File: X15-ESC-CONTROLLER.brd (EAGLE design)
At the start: 51.6 x 34.2 mm, 29 parts, among them IC1 OP-AMP, J1 3V3 -SWCLK-GND-SWDIO- NRST, Y1 ECS-80-S-4X

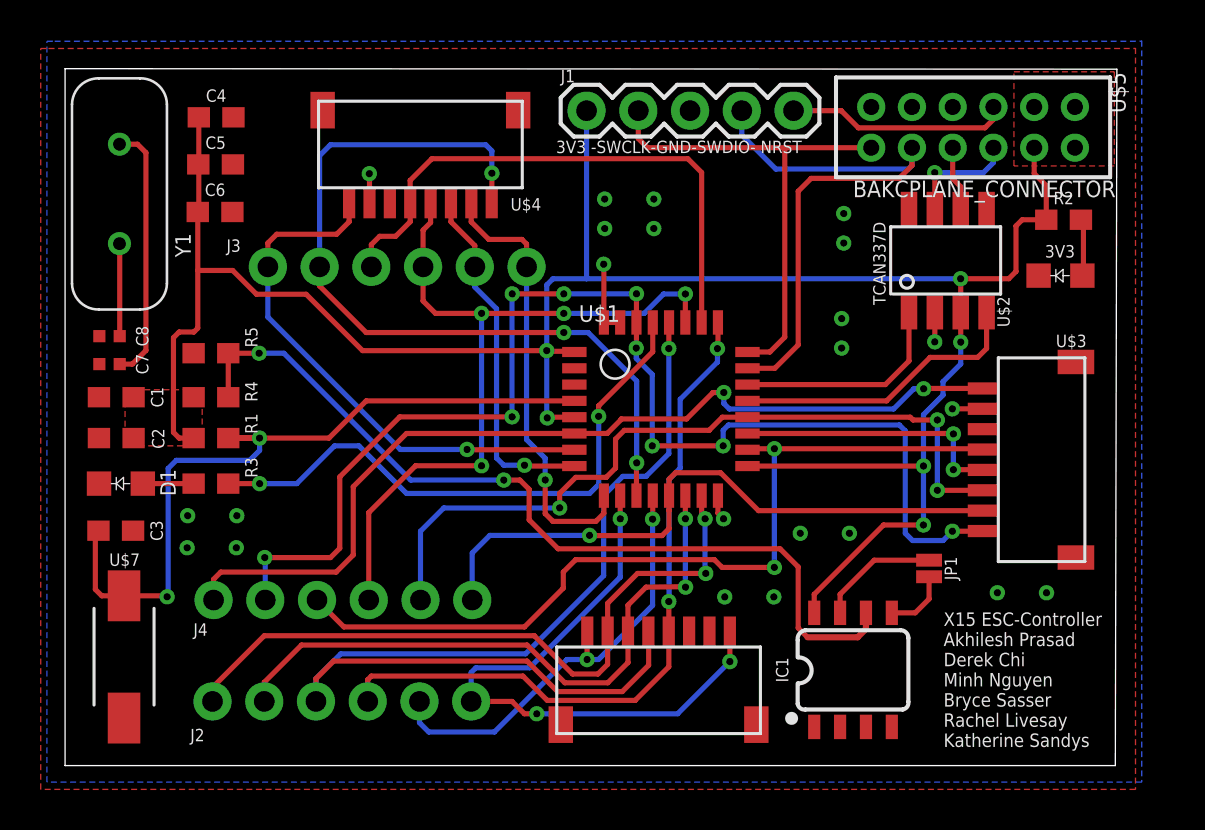
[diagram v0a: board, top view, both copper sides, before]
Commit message: Design X15 ESC Controller Again
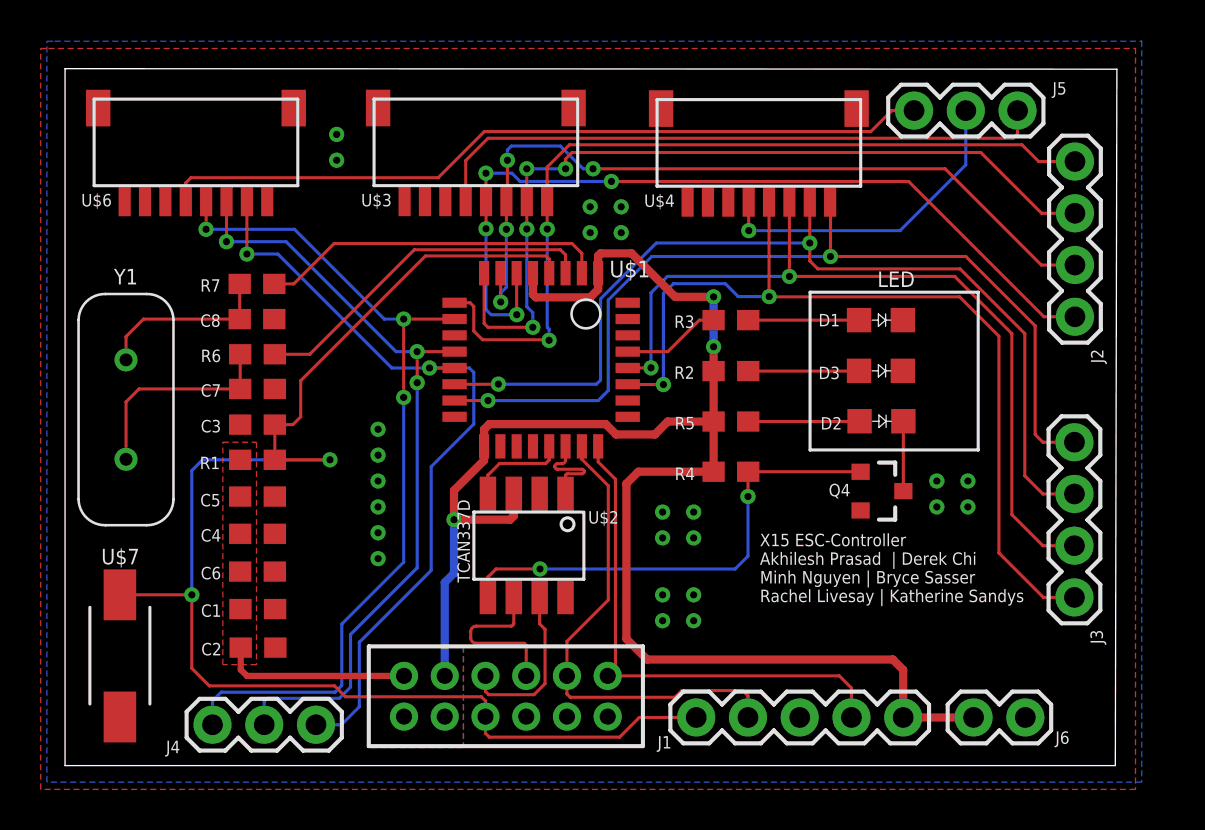
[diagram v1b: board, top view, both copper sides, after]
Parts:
- removed 3V3: COLOR, X15-ESC-Controller-Parts-Library:0805
- removed IC1: OP-AMP, SparkFun-IC-Amplifiers:SO08
- removed JP1: JUMPER-SMT, SparkFun-Jumpers:SMT-JUMPER_2_NO_NO-SILK
- added D2: FAULT, LED-0805:0805
- added D3: PWR, X15-ESC-Controller-Parts-Library:0805
- added J5: (no value), SparkFun-Connectors:1X03
- added J6: (no value), SparkFun-Connectors:1X02
- added Q4: 220mA/50V/3.5Ω, SparkFun-DiscreteSemi:SOT23-3
- added R6, R7: 0, SparkFun-Resistors:0603
- C1, C4, C5, C6: value 0.1uF -> 0.1u
- C2, C3: value 4.7uF -> 4.7u
- C7, C8: value 20pF -> 20p; device SparkFun-Capacitors:0402-TIGHT -> SparkFun-Capacitors:0603
- D1: value COLOR -> PROG
- J1: value 3V3 -SWCLK-GND-SWDIO- NRST -> (none); device X15-ESC-Controller-Parts-Library:1X05 -> SparkFun-Connectors:1X05
- J2, J3: device SparkFun-Connectors:1X06_NO_SILK -> SparkFun-Connectors:1X04
- J4: device SparkFun-Connectors:1X06_NO_SILK -> SparkFun-Connectors:1X03
- R3: value 470 -> 150
- R5: value 3.3k -> 100
- moved J3 42.8 mm to (49.6, 8.26), turned to 90 degrees
- moved U$6 39.8 mm to (1.43, 28.5), turned to 0 degrees
- moved D1 38.2 mm to (40.1, 21.9), turned to 180 degrees
- moved U$5 36.1 mm to (21.6, 3.40), turned to 270 degrees
- moved J2 35.1 mm to (49.6, 22.0), turned to 90 degrees
- moved U$3 31.8 mm to (15.2, 28.5), turned to 0 degrees
- moved J1 30.3 mm to (31.0, 2.36)
- moved R3 26.8 mm to (32.7, 21.9), turned to 0 degrees
- moved R4 25.8 mm to (32.7, 14.4)
- moved R5 25.7 mm to (32.7, 16.9), turned to 180 degrees
- moved C4 20.5 mm to (9.45, 11.4)
- moved U$2 19.1 mm to (24.6, 13.3), turned to 270 degrees
- moved R2 17.9 mm to (32.7, 19.4)
- moved C6 17.8 mm to (9.45, 9.53)
- moved U$4 16.6 mm to (29.1, 28.4)
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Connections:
- net CAN_H renamed CAN_P
- net CAN_L renamed CAN_N
- net N$4 renamed PROG_LED
- removed net ADC_IN0: J4.1, U$1.PA0, U$3.1
- removed net ADC_IN1: J3.1, U$1.PA1, U$4.1
- removed net ADC_IN4: J2.1, U$1.PA4, U$6.1
- removed net ESC_ID: U$5.12
- removed net N$12: U$2.FAULT
- removed net N$6: C7.1, Y1.2
- removed net N$9: U$2.S
- removed net TIM1_CH1: J4.3, U$1.PA8, U$3.4
- removed net TIM1_CH2: U$1.PA9, U$3.5
- removed net TIM1_CH3: J4.5, U$1.PA10, U$3.6
- removed net TLM: IC1.7, JP1.2
- removed net TLM_ESC: IC1.5, JP1.1
- new net FAULT: Q4.1, R4.1, U$2.FAULT
- new net N$4: C7.1, R6.1, Y1.2
- new net OSC_IN: R7.2, U$1.PF0-OSC_IN
- new net OSC_OUT: R6.2, U$1.PF1-OSC_OUT
- new net TIM14_CH1: J4.1, U$1.PA4, U$6.5
- new net TIM3_CH1: J3.1, U$1.PB4, U$4.5
- net +3V3: now also J1.5, J6.2, R5.2; no longer IC1.8, J1.1
- net GND: now also D3.C, J6.1, Q4.2, U$3.MECH1, U$3.MECH2, U$4.MECH1, U$4.MECH2, U$6.MECH1, U$6.MECH2; no longer 3V3.C, IC1.4, R5.1
- net N$1: now also D3.A; no longer 3V3.A
- net N$2: now also D2.C, Q4.3; no longer C3.1, R1.1, U$1.NRST, U$7.2
- net N$3: now also D2.A, R5.1; no longer IC1.6, R4.1, R5.2
- net N$7: now also R7.1
- net NRST: now also C3.1, J1.1, R1.1, U$1.NRST, U$7.2; no longer J1.5
- net SWCLK: now also J1.4; no longer J1.2
- net SWDIO: now also J1.2; no longer J1.4
- net TIM16_CH1: now also J4.2, U$1.PA6, U$6.6; no longer J2.3, U$1.PA15, U$6.4
- net TIM17_CH1: now also J4.3, U$6.7; no longer J4.6, U$3.7
- net TIM2_CH1: now also J2.1, U$1.PA0, U$3.5; no longer J3.3, U$1.PB3, U$4.4
- net TIM2_CH2: now also J2.2, U$1.PA1, U$3.6; no longer J3.4, J4.4, U$1.PB4, U$4.5
- net TIM2_CH3: now also J2.3, U$3.7; no longer J3.5, U$4.6
- net TIM2_CH4: now also J2.4, U$3.8; no longer J3.6, U$4.7
- net TIM3_CH2: now also J3.2, U$4.6; no longer J2.4, U$6.5
- net TIM3_CH3: now also J3.3, U$4.7; no longer J2.5, U$6.6
- net TIM3_CH4: now also J3.4, U$4.8; no longer J2.6, U$6.7
- net TLM_1: now also J5.1, U$3.4; no longer J4.2, U$1.PB7, U$3.8
- net TLM_2: now also J5.2, U$4.4; no longer J3.2, U$1.PA5, U$4.8
- net TLM_3: now also J5.3, U$6.4; no longer J2.2, U$1.PA6, U$6.8
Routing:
- net NRST: track 10.9 -> 70.9 mm, vias 0 -> 2
- net ADC_IN0: track 45.6 -> 0.00 mm, vias 2 -> 0
- net TIM3_CH1: track 0.00 -> 43.9 mm, vias 0 -> 2
- net TIM14_CH1: track 0.00 -> 42.5 mm, vias 0 -> 3
- net TIM1_CH1: track 42.4 -> 0.00 mm, vias 2 -> 0
- net TIM1_CH3: track 38.1 -> 0.00 mm, vias 3 -> 0
- net N$3: track 42.8 -> 5.47 mm, vias 2 -> 0
- net N$2: track 37.7 -> 3.43 mm, vias 2 -> 0
- net TLM_1: track 61.7 -> 30.8 mm, vias 9 -> 0
- net ADC_IN4: track 30.2 -> 0.00 mm, vias 3 -> 0
- net ADC_IN1: track 26.7 -> 0.00 mm, vias 1 -> 0
- net TLM_2: track 40.9 -> 16.1 mm, vias 3 -> 1
- net PROG_LED: track 29.2 -> 4.86 mm, vias 2 -> 0
- net TIM2_CH3: track 17.4 -> 41.6 mm, vias 1 -> 4
- net FAULT: track 0.00 -> 23.8 mm, vias 0 -> 2
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- added copper zone on layer 16, net +3V3
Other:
- board text added: "LED"
- board text added: "X15 ESC-Controller Akhilesh Prasad | Derek Chi Minh Nguyen | Bryce Sasser Rachel Livesay | Katherine Sandys"
- board text removed: "X15 ESC-Controller Akhilesh Prasad Derek Chi Minh Nguyen Bryce Sasser Rachel Livesay Katherine Sandys"

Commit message: Fix New Version of X15-ESC Controller
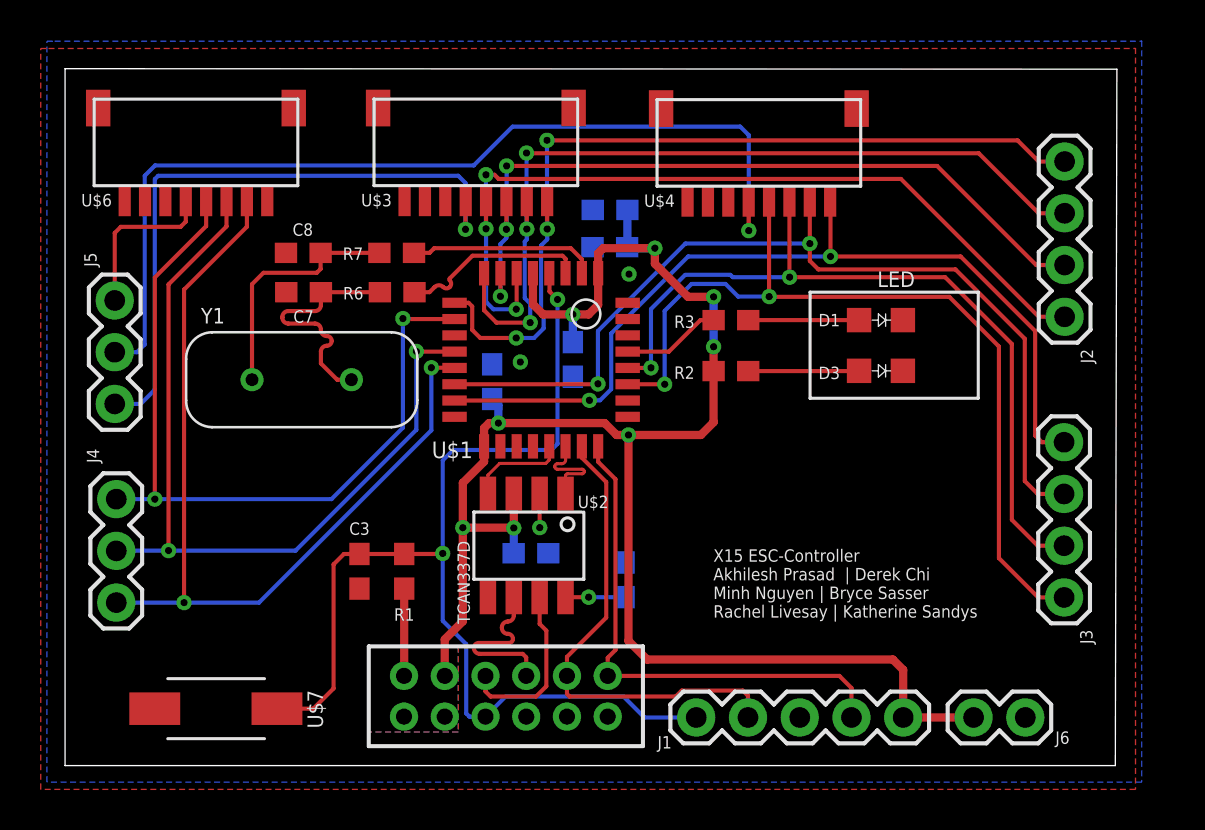
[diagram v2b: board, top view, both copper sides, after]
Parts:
- removed D2: FAULT, LED-0805:0805
- removed Q4: 220mA/50V/3.5Ω, SparkFun-DiscreteSemi:SOT23-3
- removed R5: 100, SparkFun-Resistors:0603
- R4: value 1k -> 0
- moved J5 46.6 mm to (2.44, 17.8), turned to 90 degrees
- moved C2 26.2 mm to (26.7, 25.5), flipped to the bottom, turned to 180 degrees
- moved C1 26.1 mm to (26.8, 27.3), flipped to the bottom
- moved C5 16.9 mm to (24.9, 19.9), flipped to the bottom, turned to 270 degrees
- moved C4 13.7 mm to (21.0, 18.8), flipped to the bottom, turned to 90 degrees
- moved C6 13.5 mm to (22.9, 10.4), flipped to the bottom
- moved J4 12.0 mm to (2.51, 13.1), turned to 270 degrees
- moved R1 9.05 mm to (16.6, 9.54), turned to 270 degrees
- moved C3 8.77 mm to (14.5, 9.54), turned to 270 degrees
- moved Y1 8.75 mm to (11.6, 18.9), turned to 0 degrees
- moved R6 7.50 mm to (16.3, 23.2)
- moved R4 7.44 mm to (27.5, 9.12), flipped to the bottom, turned to 270 degrees
- moved R7 7.03 mm to (16.3, 25.2)
- moved U$7 5.38 mm to (7.40, 2.79), turned to 0 degrees
- moved C7 5.26 mm to (11.7, 23.2), turned to 180 degrees
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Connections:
- removed net FAULT: Q4.1, R4.1, U$2.FAULT
- removed net N$3: D2.A, R5.1
- net +3V3: now also C2.2, C5.1, C6.2; no longer C2.1, C5.2, C6.1, R4.2, R5.2
- net GND: now also C2.1, C5.2, C6.1, R4.1; no longer C2.2, C5.1, C6.2, Q4.2
- net N$2: now also R4.2, U$2.S; no longer D2.C, Q4.3
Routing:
- net TLM_2: track 16.1 -> 46.9 mm
- net TLM_3: track 38.1 -> 8.05 mm
- net FAULT: track 23.8 -> 0.00 mm, vias 2 -> 0
- net NRST: track 70.9 -> 54.5 mm
- net OSC_OUT: track 17.4 -> 9.18 mm
- net OSC_IN: track 17.1 -> 9.25 mm
- net TIM17_CH1: track 38.6 -> 44.2 mm
- net N$3: track 5.47 -> 0.00 mm
- net TIM14_CH1: track 42.5 -> 39.1 mm, vias 3 -> 2
- net N$7: track 8.81 -> 12.0 mm
- net TIM16_CH1: track 38.9 -> 41.3 mm, vias 3 -> 2
- net GND: track 0.00 -> 1.67 mm, vias 24 -> 3
- net TIM3_CH4: track 45.6 -> 43.9 mm
- net N$4: track 10.4 -> 11.8 mm
- net TIM3_CH3: track 47.4 -> 46.1 mm
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
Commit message: Complete New Version of X15 ESC Controller Board
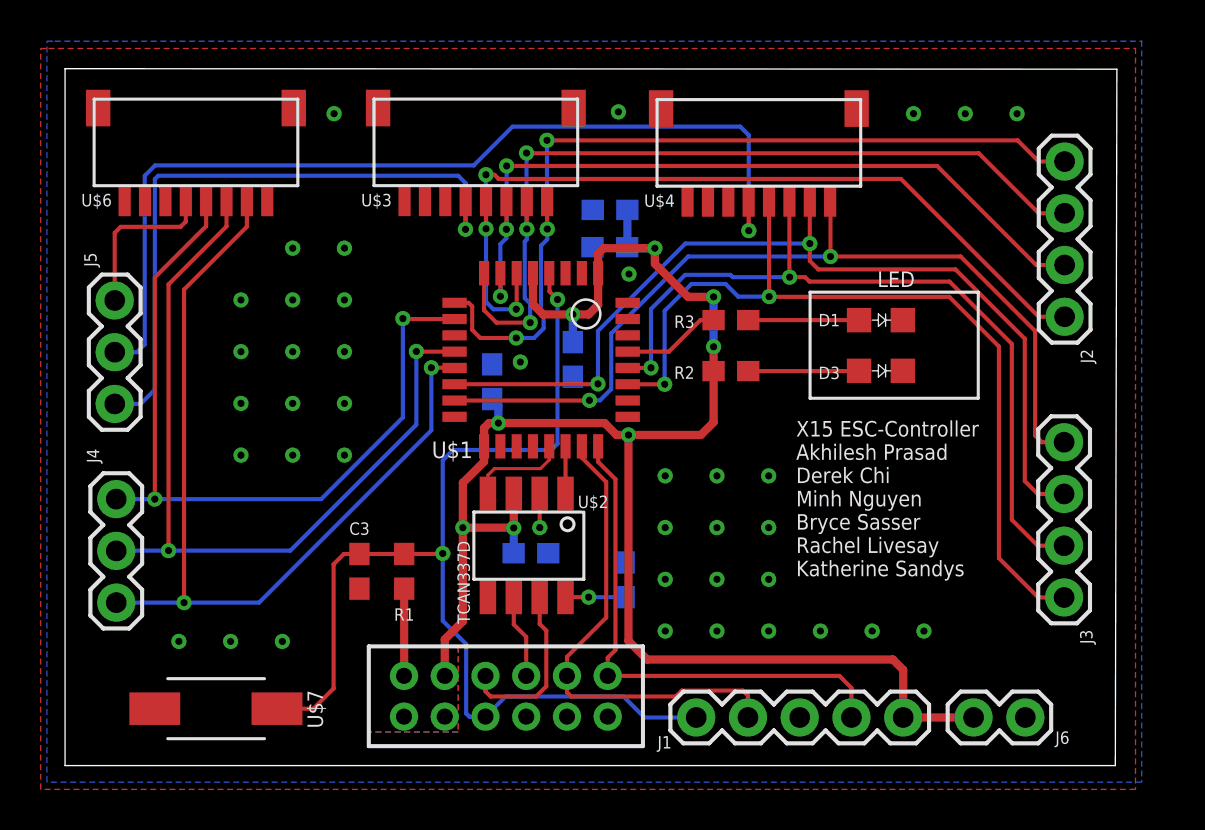
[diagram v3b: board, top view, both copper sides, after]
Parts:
- removed C7, C8: 20p, SparkFun-Capacitors:0603
- removed R6, R7: 0, SparkFun-Resistors:0603
- removed Y1: ECS-80-S-4X, X15-ESC-Controller-Parts-Library:XTAL_ECS-80-S-4X
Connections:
- removed net N$4: C7.1, R6.1, Y1.2
- removed net N$7: C8.1, R7.1, Y1.1
- net GND: no longer C7.2, C8.2
- net OSC_IN: no longer R7.2
- net OSC_OUT: no longer R6.2
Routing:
- net N$7: track 12.0 -> 0.00 mm
- net N$4: track 11.8 -> 0.00 mm
- net OSC_IN: track 9.25 -> 0.00 mm
- net OSC_OUT: track 9.18 -> 0.00 mm
- net CAN_N: track 8.29 -> 4.12 mm
- net CAN_TX: track 4.77 -> 2.32 mm
- net GND: vias 3 -> 40
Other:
- board text added: "X15 ESC-Controller Akhilesh Prasad Derek Chi Minh Nguyen Bryce Sasser Rachel Livesay Katherine Sandys"
- board text removed: "X15 ESC-Controller Akhilesh Prasad | Derek Chi Minh Nguyen | Bryce Sasser Rachel Livesay | Katherine Sandys"

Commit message: Minor Change
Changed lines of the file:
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@@
 </element>
 <element name="R1" library="SparkFun-Resistors" package="0603" value="1k" x="16.6497" y="9.5377" smashed="yes" rot="R270">
-<attribute name="NAME" x="16.6497" y="7.7216" size="0.6096" layer="25" ratio="20" rot="R180" align="bottom-center"/>
+<attribute name="NAME" x="16.6497" y="11.303" size="0.6096" layer="25" ratio="20" align="bottom-center"/>
 <attribute name="PROD_ID" value="RES-07856" x="19.1389" y="12.6365" size="1.778" layer="27" rot="R270" display="off"/>
-<attribute name="VALUE" x="16.6497" y="11.2776" size="0.6096" layer="27" ratio="20" rot="R180" align="top-center"/>
+<attribute name="VALUE" x="16.6497" y="7.2136" size="0.6096" layer="27" ratio="20" rot="R180" align="top-center"/>
 </element>
 <element name="U$7" library="X15-ESC-Controller-Parts-Library" package="DISCRETECOMPONENTS_SW_2512" package3d_urn="urn:adsk.eagle:package:24384574/2" value="" x="7.4041" y="2.794" smashed="yes">
